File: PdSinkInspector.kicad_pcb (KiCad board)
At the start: 2 copper layers, 60 x 40 mm, 2 parts, among them IC1 632723100011, U1 RP2040

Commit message: [Update]RP2040を結線
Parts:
- added C1: 0.1u, Capacitor_SMD:C_0603_1608Metric, F.Cu at (137.2, 48.0)
- added C10: 0.1u, Capacitor_SMD:C_0603_1608Metric, F.Cu at (141.2, 55.5)
- added C11: 1u, Capacitor_SMD:C_0603_1608Metric, F.Cu at (141.2, 58.0)
- added C2: 0.1u, Capacitor_SMD:C_0603_1608Metric, F.Cu at (137.2, 50.5)
- added C3: 0.1u, Capacitor_SMD:C_0603_1608Metric, F.Cu at (137.2, 53.0)
- added C4: 0.1u, Capacitor_SMD:C_0603_1608Metric, F.Cu at (137.2, 55.5)
- added C5: 0.1u, Capacitor_SMD:C_0603_1608Metric, F.Cu at (137.2, 58.0)
- added C6: 0.1u, Capacitor_SMD:C_0603_1608Metric, F.Cu at (137.2, 60.5)
- added C7: 0.1u, Capacitor_SMD:C_0603_1608Metric, F.Cu at (141.2, 48.0)
- added C8: 1u, Capacitor_SMD:C_0603_1608Metric, F.Cu at (141.2, 50.5)
- added C9: 0.1u, Capacitor_SMD:C_0603_1608Metric, F.Cu at (141.2, 53.0)
- added H1: MountingHole, MountingHole:MountingHole_3.2mm_M3, F.Cu at (100.9, 81.8)
- added H2: MountingHole, MountingHole:MountingHole_3.2mm_M3, F.Cu at (100.9, 89.8)
- added H3: MountingHole, MountingHole:MountingHole_3.2mm_M3, F.Cu at (100.9, 97.8)
- added H4: MountingHole, MountingHole:MountingHole_3.2mm_M3, F.Cu at (100.9, 105.7)
- added IC2: STUSB4700YQTR, TE-01:QFN50P400X400X90-25N-D, F.Cu at (108.0, 80.8)
- added R1: 27, Resistor_SMD:R_0603_1608Metric, F.Cu at (106.9, 84.9)
- added R2: 27, Resistor_SMD:R_0603_1608Metric, F.Cu at (106.9, 87.4)
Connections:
- IC1 pad A1: unconnected-(IC1-GND_1-PadA1) -> GND
- IC1 pad A12: unconnected-(IC1-GND_2-PadA12) -> GND
- IC1 pad A5: unconnected-(IC1-CC1-PadA5) -> Net-(IC1-CC1)
- IC1 pad A6: unconnected-(IC1-DP1-PadA6) -> USB_D+
- IC1 pad A7: unconnected-(IC1-DN1-PadA7) -> USB_D-
- IC1 pad B1: unconnected-(IC1-GND_3-PadB1) -> GND
- IC1 pad B12: unconnected-(IC1-GND_4-PadB12) -> GND
- IC1 pad B5: unconnected-(IC1-CC2-PadB5) -> Net-(IC1-CC2)
- IC1 pad B6: unconnected-(IC1-DP2-PadB6) -> USB_D+
- IC1 pad B7: unconnected-(IC1-DN2-PadB7) -> USB_D-
- IC1 pad G1: unconnected-(IC1-GND_5-PadG1) -> GND
- IC1 pad G2: unconnected-(IC1-GND_6-PadG2) -> GND
- U1 pad 1: Net-(U1-IOVDD-Pad1) -> +3.3V
- U1 pad 10: Net-(U1-IOVDD-Pad1) -> +3.3V
- U1 pad 19: unconnected-(U1-TESTEN-Pad19) -> GND
- U1 pad 22: Net-(U1-IOVDD-Pad1) -> +3.3V
- U1 pad 23: Net-(U1-DVDD-Pad23) -> +1V1
- U1 pad 33: Net-(U1-IOVDD-Pad1) -> +3.3V
- U1 pad 42: Net-(U1-IOVDD-Pad1) -> +3.3V
- U1 pad 43: unconnected-(U1-ADC_AVDD-Pad43) -> +3.3V
- U1 pad 44: unconnected-(U1-VREG_IN-Pad44) -> +3.3V
- U1 pad 45: unconnected-(U1-VREG_VOUT-Pad45) -> +1V1
- U1 pad 46: unconnected-(U1-USB_DM-Pad46) -> Net-(U1-USB_DM)
- U1 pad 47: unconnected-(U1-USB_DP-Pad47) -> Net-(U1-USB_DP)
- U1 pad 48: unconnected-(U1-USB_VDD-Pad48) -> +3.3V
- U1 pad 49: Net-(U1-IOVDD-Pad1) -> +3.3V
- U1 pad 50: Net-(U1-DVDD-Pad23) -> +1V1
- U1 pad 57: unconnected-(U1-GND-Pad57) -> GND
- U1 pad 8: unconnected-(U1-GPIO6-Pad8) -> I2C1_SDA
- U1 pad 9: unconnected-(U1-GPIO7-Pad9) -> I2C1_SCL

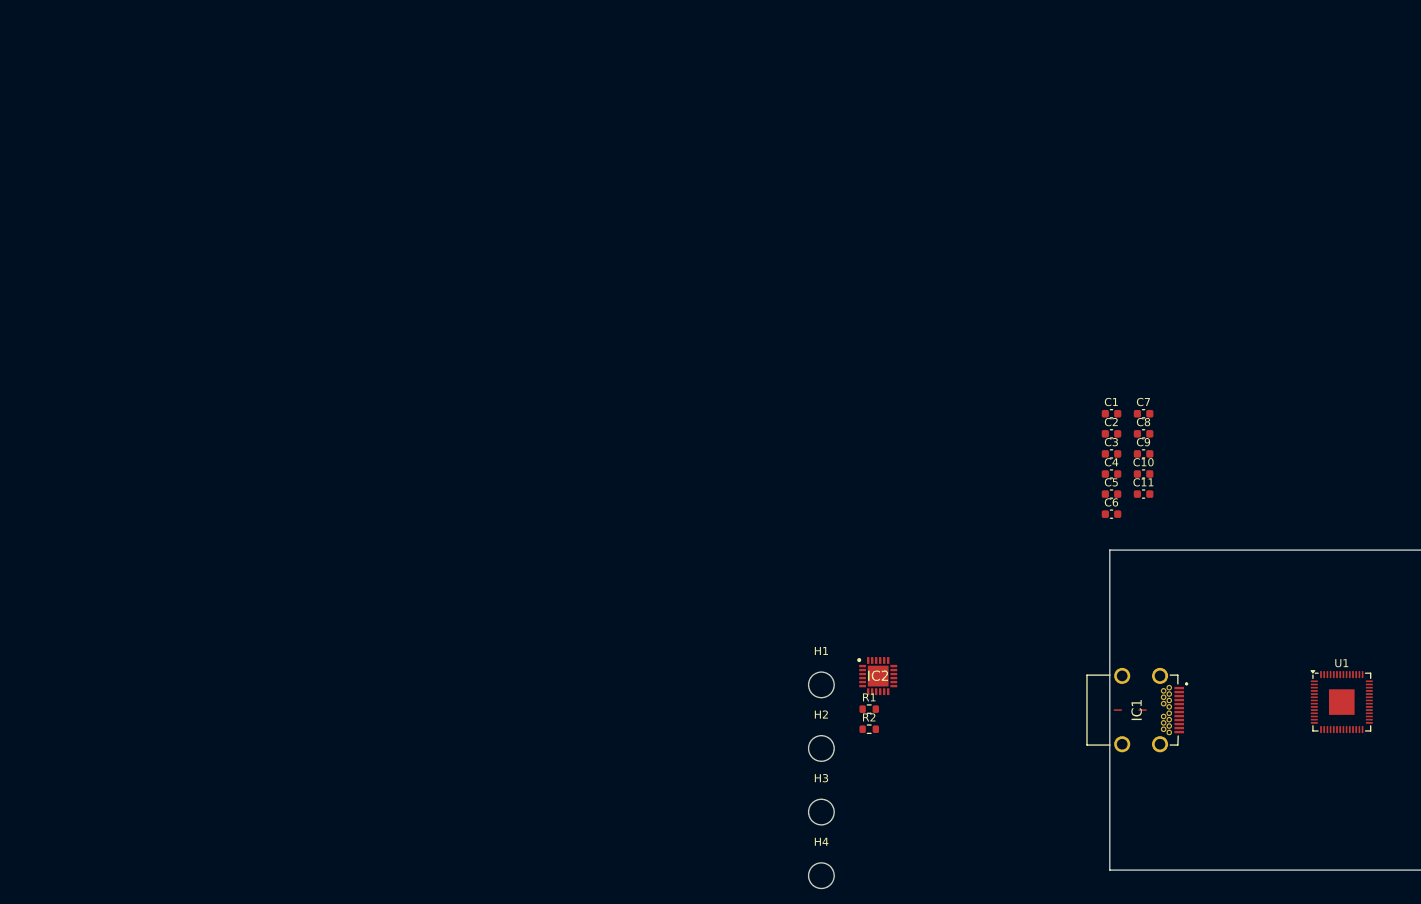
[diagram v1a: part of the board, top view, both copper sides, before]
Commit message: LDO、Flash追加
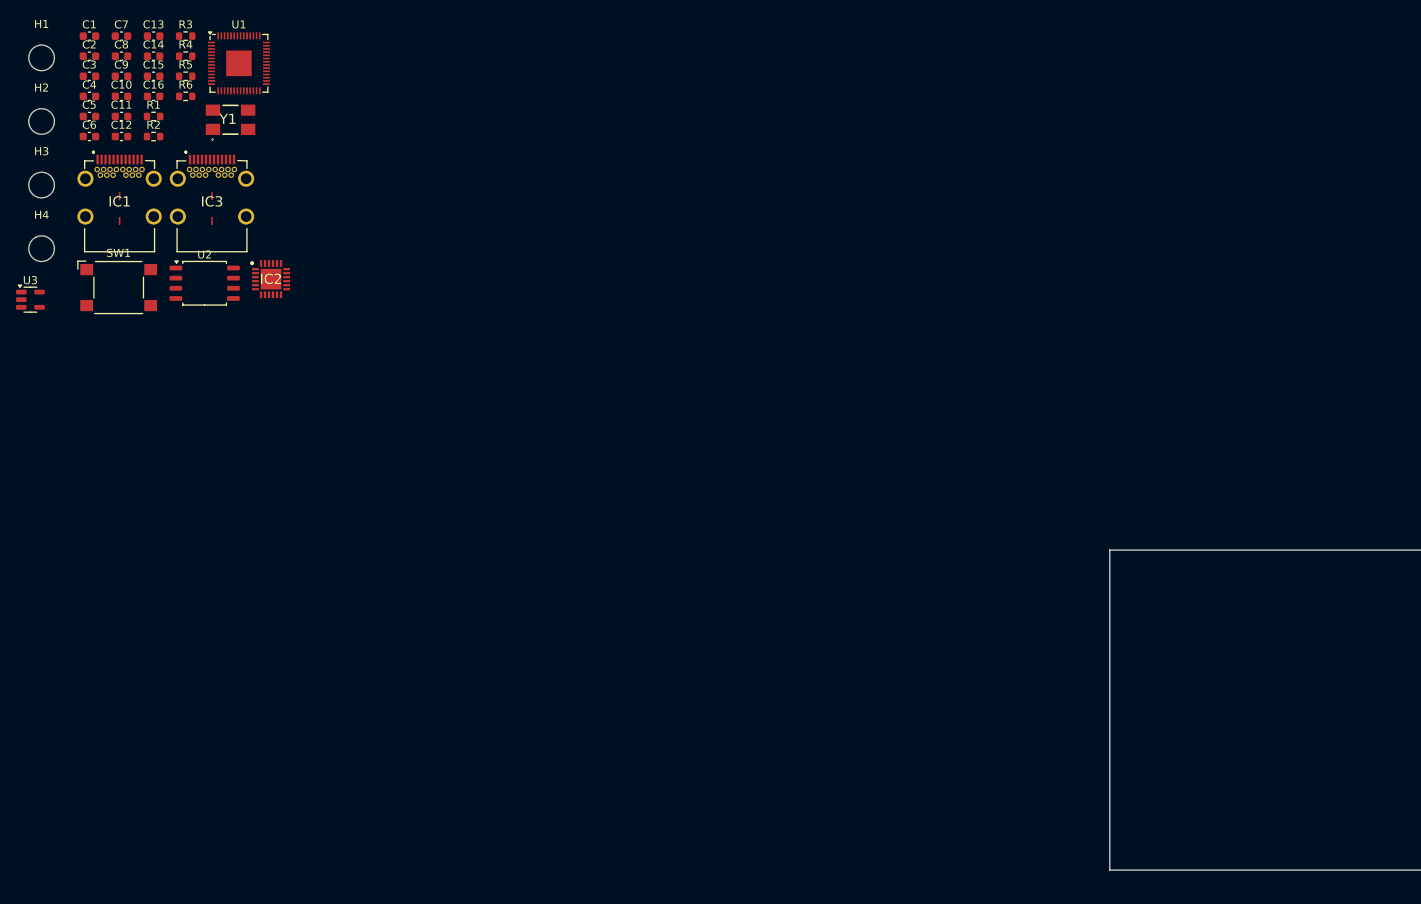
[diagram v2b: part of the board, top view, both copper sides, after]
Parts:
- added C12: 0.1u, Capacitor_SMD:C_0603_1608Metric, F.Cu at (13.5, 13.3)
- added C13: 0.1u, Capacitor_SMD:C_0603_1608Metric, F.Cu at (17.5, 0.76)
- added C14: 0.1u, Capacitor_SMD:C_0603_1608Metric, F.Cu at (17.5, 3.27)
- added C15: 27p, Capacitor_SMD:C_0603_1608Metric, F.Cu at (17.5, 5.78)
- added C16: 27p, Capacitor_SMD:C_0603_1608Metric, F.Cu at (17.5, 8.29)
- added IC3: 632723100011, TE-01:632723100011, F.Cu at (24.8, 21.5)
- added R3: NC, Resistor_SMD:R_0603_1608Metric, F.Cu at (21.5, 0.76)
- added R4: 27, Resistor_SMD:R_0603_1608Metric, F.Cu at (21.5, 3.27)
- added R5: NC, Resistor_SMD:R_0603_1608Metric, F.Cu at (21.5, 5.78)
- added R6: 1k, Resistor_SMD:R_0603_1608Metric, F.Cu at (21.5, 8.29)
- added SW1: SW_Omron_B3FS, Button_Switch_SMD:SW_SPST_Omron_B3FS-105xP, F.Cu at (13.1, 32.2)
- added U2: W25Q128JVS, Package_SO:SOIC-8_5.23x5.23mm_P1.27mm, F.Cu at (23.9, 31.6)
- added U3: TLV75733PDBV, Package_TO_SOT_SMD:SOT-23-5, F.Cu at (2.08, 33.7)
- added Y1: ABMM2-12.000MHZ-E2-T, TE-01:ABMM2, F.Cu at (27.1, 11.2)
- moved U1 159.3 mm to (28.1, 4.16)
- moved IC1 142.2 mm to (13.2, 21.5), turned to 0 degrees
- moved C1 136.2 mm to (9.46, 0.76)
- moved C10 136.2 mm to (13.5, 8.29)
- moved C11 136.2 mm to (13.5, 10.8)
- moved C2 136.2 mm to (9.46, 3.27)
- moved C3 136.2 mm to (9.46, 5.78)
- moved C4 136.2 mm to (9.46, 8.29)
- moved C5 136.2 mm to (9.46, 10.8)
- moved C6 136.2 mm to (9.46, 13.3)
- moved C7 136.2 mm to (13.5, 0.76)
- moved C8 136.2 mm to (13.5, 3.27)
- moved C9 136.2 mm to (13.5, 5.78)
- moved H1 125.1 mm to (3.48, 3.48)
- moved H2 125.1 mm to (3.48, 11.4)
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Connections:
- IC1 pad A6: USB_D+ -> unconnected-(IC1-DP1-PadA6)
- IC1 pad A7: USB_D- -> unconnected-(IC1-DN1-PadA7)
- IC1 pad B6: USB_D+ -> unconnected-(IC1-DP2-PadB6)
- IC1 pad B7: USB_D- -> unconnected-(IC1-DN2-PadB7)
- IC2 pad 7: unconnected-(IC2-SCL-Pad7) -> I2C1_SCL
- IC2 pad 8: unconnected-(IC2-SDA-Pad8) -> I2C1_SDA
- U1 pad 20: unconnected-(U1-XIN-Pad20) -> X_IN
- U1 pad 21: unconnected-(U1-XOUT-Pad21) -> X_OUT
- U1 pad 51: unconnected-(U1-QSPI_SD3-Pad51) -> Net-(U1-QSPI_SD3)
- U1 pad 52: unconnected-(U1-QSPI_SCLK-Pad52) -> Net-(U1-QSPI_SCLK)
- U1 pad 53: unconnected-(U1-QSPI_SD0-Pad53) -> Net-(U1-QSPI_SD0)
- U1 pad 54: unconnected-(U1-QSPI_SD2-Pad54) -> Net-(U1-QSPI_SD2)
- U1 pad 55: unconnected-(U1-QSPI_SD1-Pad55) -> Net-(U1-QSPI_SD1)
- U1 pad 56: unconnected-(U1-QSPI_SS-Pad56) -> Net-(U1-QSPI_SS)

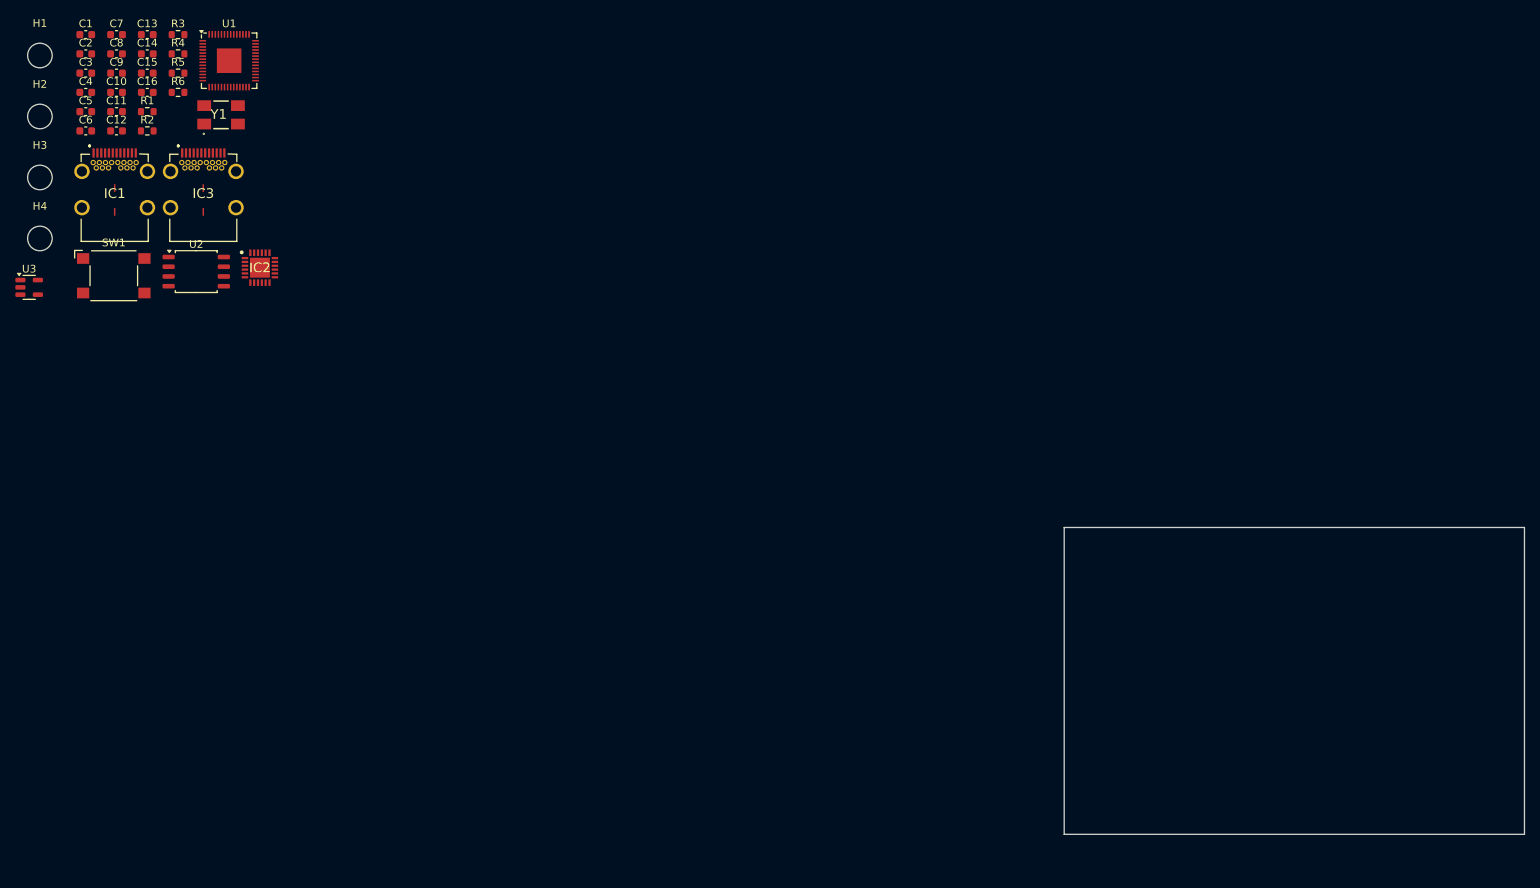
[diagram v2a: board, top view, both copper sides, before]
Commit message: i2cにプルアップ追加+JLC用にBOM作成(途中)
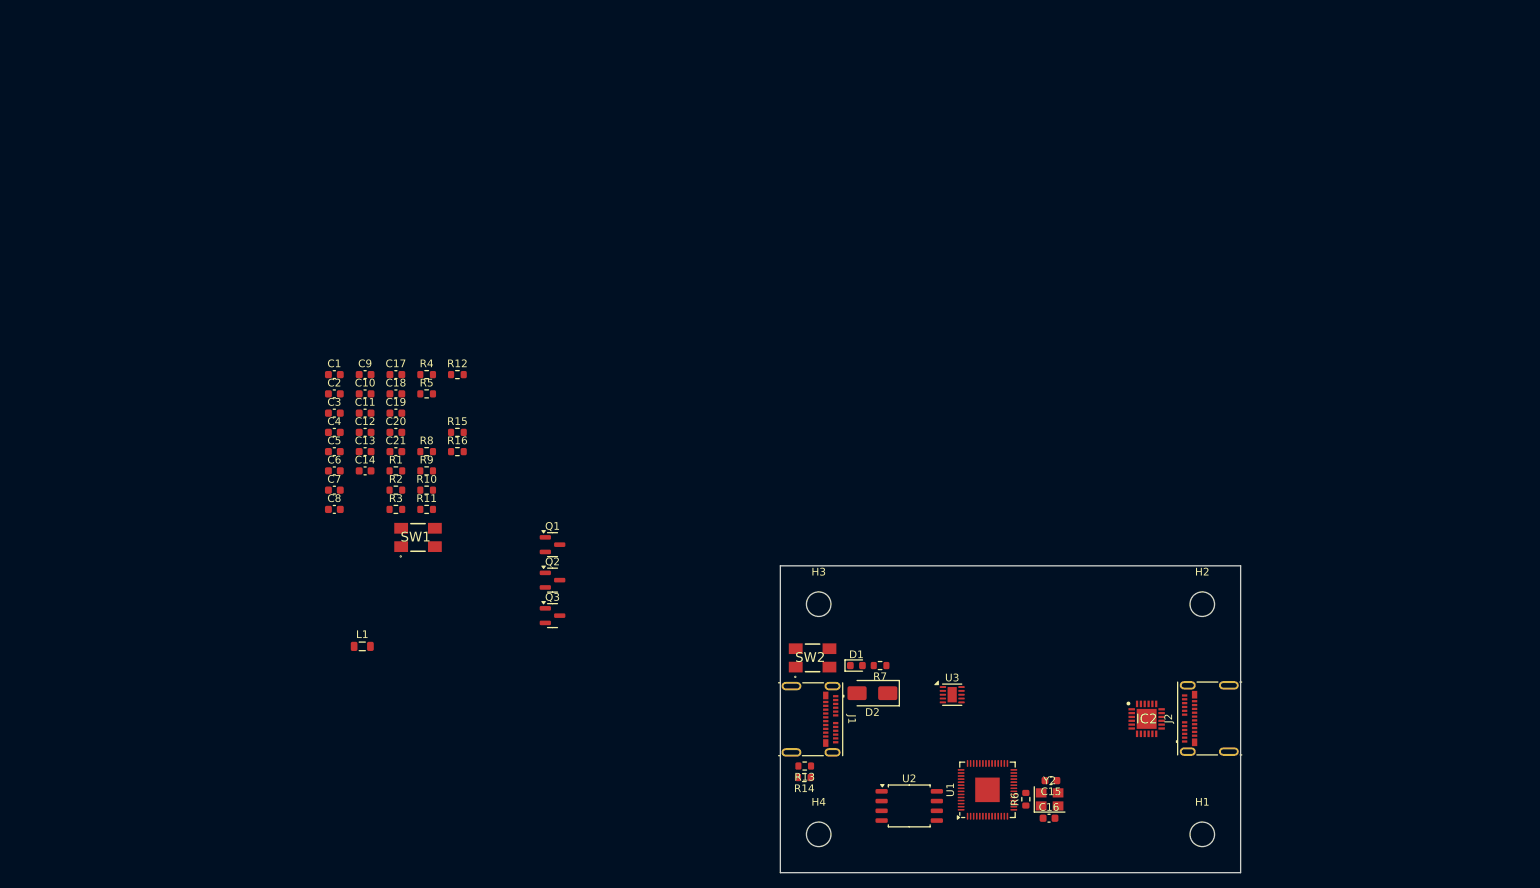
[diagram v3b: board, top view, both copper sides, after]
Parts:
- removed IC1, IC3: 632723100011, TE-01:632723100011
- removed Y1: ABMM2-12.000MHZ-E2-T, TE-01:ABMM2
- added C17: 0.1u, Capacitor_SMD:C_0603_1608Metric, F.Cu at (49.9, 45.1)
- added C18: 10u, Capacitor_SMD:C_0603_1608Metric, F.Cu at (49.9, 47.6)
- added C19: 10u, Capacitor_SMD:C_0603_1608Metric, F.Cu at (49.9, 50.1)
- added C20: 1u, Capacitor_SMD:C_0603_1608Metric, F.Cu at (49.9, 52.6)
- added C21: 1u, Capacitor_SMD:C_0603_1608Metric, F.Cu at (49.9, 55.1)
- added D1: LED, LED_SMD:LED_0603_1608Metric, F.Cu at (109.9, 83.0)
- added D2: SS14, Diode_SMD:D_SMA, F.Cu at (112.0, 86.6)
- added J1: USB_C_Receptacle, Connector_USB:USB_C_Receptacle_Molex_105450-0101, F.Cu at (104.0, 90.0)
- added J2: USB_C_Receptacle, Connector_USB:USB_C_Receptacle_Molex_105450-0101, F.Cu at (155.9, 89.9)
- added L1: 1.5u, Inductor_SMD:L_0805_2012Metric, F.Cu at (45.5, 80.5)
- added Q1: AO3401A, Package_TO_SOT_SMD:SOT-23, F.Cu at (70.3, 67.2)
- added Q2: AO3401A, Package_TO_SOT_SMD:SOT-23, F.Cu at (70.3, 71.9)
- added Q3: AO3401A, Package_TO_SOT_SMD:SOT-23, F.Cu at (70.3, 76.5)
- added R10: 2k2, Resistor_SMD:R_0603_1608Metric, F.Cu at (53.9, 60.1)
- added R11: 10k, Resistor_SMD:R_0603_1608Metric, F.Cu at (53.9, 62.6)
- added R12: 10k, Resistor_SMD:R_0603_1608Metric, F.Cu at (57.9, 45.1)
- added R13: 5.1, Resistor_SMD:R_0603_1608Metric, F.Cu at (103.2, 96.1)
- added R14: 5.1k, Resistor_SMD:R_0603_1608Metric, F.Cu at (103.1, 97.6)
- added R15: 4.7k, Resistor_SMD:R_0603_1608Metric, F.Cu at (57.9, 52.6)
- added R16: 4.7k, Resistor_SMD:R_0603_1608Metric, F.Cu at (57.9, 55.1)
- added R7: 1k, Resistor_SMD:R_0603_1608Metric, F.Cu at (113.0, 83.0)
- added R8: 10k, Resistor_SMD:R_0603_1608Metric, F.Cu at (53.9, 55.1)
- added R9: 10k, Resistor_SMD:R_0603_1608Metric, F.Cu at (53.9, 57.6)
- added SW2: SW_MEC_5E, TE-01:ABMM2, F.Cu at (104.2, 82.0)
- added Y2: Crystal_GND24, Crystal:Crystal_SMD_3225-4Pin_3.2x2.5mm, F.Cu at (135.1, 100.5)
- C13: value 0.1u -> 10u
- R4: value 27 -> 100k
- R5: value NC -> 1k
- SW1: value SW_Omron_B3FS -> SW_MEC_5E; footprint Button_Switch_SMD:SW_SPST_Omron_B3FS-105xP -> TE-01:ABMM2
- U3: value TLV75733PDBV -> TPS63031DSK; footprint Package_TO_SOT_SMD:SOT-23-5 -> Package_SON:WSON-10-1EP_2.5x2.5mm_P0.5mm_EP1.2x2mm
- moved H1 182.4 mm to (155.0, 105.0)
- moved H2 164.3 mm to (155.0, 75.0)
- moved C16 150.9 mm to (135.0, 102.9)
- moved C15 149.6 mm to (135.3, 98.0), turned to 180 degrees
- moved R6 143.9 mm to (132.0, 100.4), turned to 90 degrees
- moved U1 137.1 mm to (127.0, 99.2), turned to 90 degrees
- moved U3 131.5 mm to (122.4, 86.8)
- moved IC2 129.7 mm to (147.8, 90.0)
- moved H4 127.8 mm to (105.0, 105.0)
- moved U2 116.1 mm to (116.8, 101.3)
- moved H3 115.8 mm to (105.0, 75.0)
- moved R3 68.1 mm to (49.9, 62.6)
- moved C8 65.8 mm to (41.9, 62.6)
- moved C7 65.8 mm to (41.9, 60.1)
- moved C13 61.3 mm to (45.9, 55.1)
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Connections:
- net X_IN renamed Net-(U1-XIN)
- C14 pad 1: +3.3V -> Net-(U3-EN)
- C16 pad 1: Net-(Y1-X2) -> Net-(C16-Pad1)
- IC2 pad 13: unconnected-(IC2-VVAR_ADDR0-Pad13) -> Net-(IC2-VVAR_ADDR0)
- IC2 pad 18: unconnected-(IC2-VBUS_SENSE-Pad18) -> Vout
- IC2 pad 19: unconnected-(IC2-VBUS_DISCH-Pad19) -> Net-(IC2-VBUS_DISCH)
- IC2 pad 20: unconnected-(IC2-VBUS_EN_SRC-Pad20) -> Net-(IC2-VBUS_EN_SRC)
- IC2 pad 21: unconnected-(IC2-VREG_1V2-Pad21) -> Net-(IC2-VREG_1V2)
- IC2 pad 22: unconnected-(IC2-VSYS-Pad22) -> VBUS
- IC2 pad 23: unconnected-(IC2-VREG_2V7-Pad23) -> Net-(IC2-VREG_2V7)
- IC2 pad 24: unconnected-(IC2-VDD-Pad24) -> VBUS
- IC2 pad 25: unconnected-(IC2-EP-Pad25) -> GND
- IC2 pad 3: unconnected-(IC2-VCONN-Pad3) -> GND
- IC2 pad 6: unconnected-(IC2-RESET-Pad6) -> GND
- R4 pad 2: Net-(IC3-CC2) -> Net-(IC2-VVAR_ADDR0)
- R6 pad 1: X_OUT -> Net-(C16-Pad1)
- R6 pad 2: Net-(Y1-X2) -> Net-(U1-XOUT)
- SW1 pad 1: unconnected-(SW1-Pad1) -> RESET
- SW1 pad 2: unconnected-(SW1-Pad2) -> RESET
- U1 pad 21: X_OUT -> Net-(U1-XOUT)
- U1 pad 26: unconnected-(U1-RUN-Pad26) -> RESET
- U3 pad 1: VBUS -> +3.3V
- U3 pad 2: GND -> Net-(U3-L2)
- U3 pad 3: 3.3V_EN -> GND
- U3 pad 4: unconnected-(U3-NC-Pad4) -> Net-(U3-L1)
- U3 pad 5: +3.3V -> VBUS

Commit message: [Update]基板配置してみた
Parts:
- added D3: D, Diode_SMD:D_SOD-882, F.Cu at (109.8, 85.4)
- added D4: D, Diode_SMD:D_SOD-882, F.Cu at (109.4, 90.5)
- added D5: D, Diode_SMD:D_SOD-882, F.Cu at (109.4, 92.7)
- added R17: NC, Resistor_SMD:R_0603_1608Metric, F.Cu at (133.9, 104.5)
- R13: value 5.1 -> 5.1k
- moved R4 106.9 mm to (143.9, 102.8)
- moved C9 104.2 mm to (134.3, 100.1)
- moved C1 103.9 mm to (125.2, 107.1), turned to -90 degrees
- moved C20 102.8 mm to (143.4, 95.2), turned to 90 degrees
- moved C11 100.9 mm to (134.3, 98.6)
- moved C21 100.4 mm to (141.9, 95.2), turned to 90 degrees
- moved R9 98.6 mm to (146.4, 91.6), turned to 90 degrees
- moved R10 97.6 mm to (144.9, 95.2), turned to 90 degrees
- moved R12 94.1 mm to (141.6, 88.2), turned to 180 degrees
- moved C10 93.4 mm to (121.8, 101.9), turned to 180 degrees
- moved C8 93.1 mm to (123.7, 107.1), turned to -90 degrees
- moved C4 92.4 mm to (121.8, 98.9), turned to 180 degrees
- moved C2 91.9 mm to (121.8, 92.9), turned to 180 degrees
- moved C5 91.9 mm to (121.8, 100.4), turned to 180 degrees
- moved C3 91.4 mm to (121.8, 94.4), turned to 180 degrees
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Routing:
- net Net-(U1-USB_DP): track 0.00 -> 17.1 mm, vias 0 -> 2
- net Net-(U1-QSPI_SD2): track 0.00 -> 16.0 mm
- net Net-(U1-USB_DM): track 0.00 -> 15.8 mm, vias 0 -> 2
- net Net-(U1-XIN): track 0.00 -> 8.48 mm
- net Net-(U1-QSPI_SD0): track 0.00 -> 7.89 mm
- net Net-(U1-QSPI_SCLK): track 0.00 -> 7.53 mm
- net Net-(U1-QSPI_SD3): track 0.00 -> 7.17 mm
- net Net-(U1-XOUT): track 0.00 -> 6.07 mm
- net +1V1: track 0.00 -> 5.97 mm
- net USB_D-: track 0.00 -> 4.41 mm
- net USB_D+: track 0.00 -> 4.11 mm
- net Net-(C16-Pad1): track 0.00 -> 3.95 mm
- net I2C1_SDA: track 0.00 -> 2.42 mm
- net I2C1_SCL: track 0.00 -> 1.96 mm
- net Net-(D2-A): track 0.00 -> 1.40 mm
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- added copper zone on B.Cu, net GND
- added copper zone on F.Cu, net GND
